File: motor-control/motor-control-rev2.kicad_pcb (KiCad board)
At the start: 2 copper layers, 122.3 x 65.9 mm, 80 parts, among them P1 CONN_02X12, P2 to_motor_phase_1, P3 to_motor_phase_2, P4 to_motor_phase_3, P5 CONN_01X01, P6 CONN_01X01, P7 CONN_01X04, Q1 csd19505kcs, Q10 csd19505kcs, Q11 csd19505kcs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

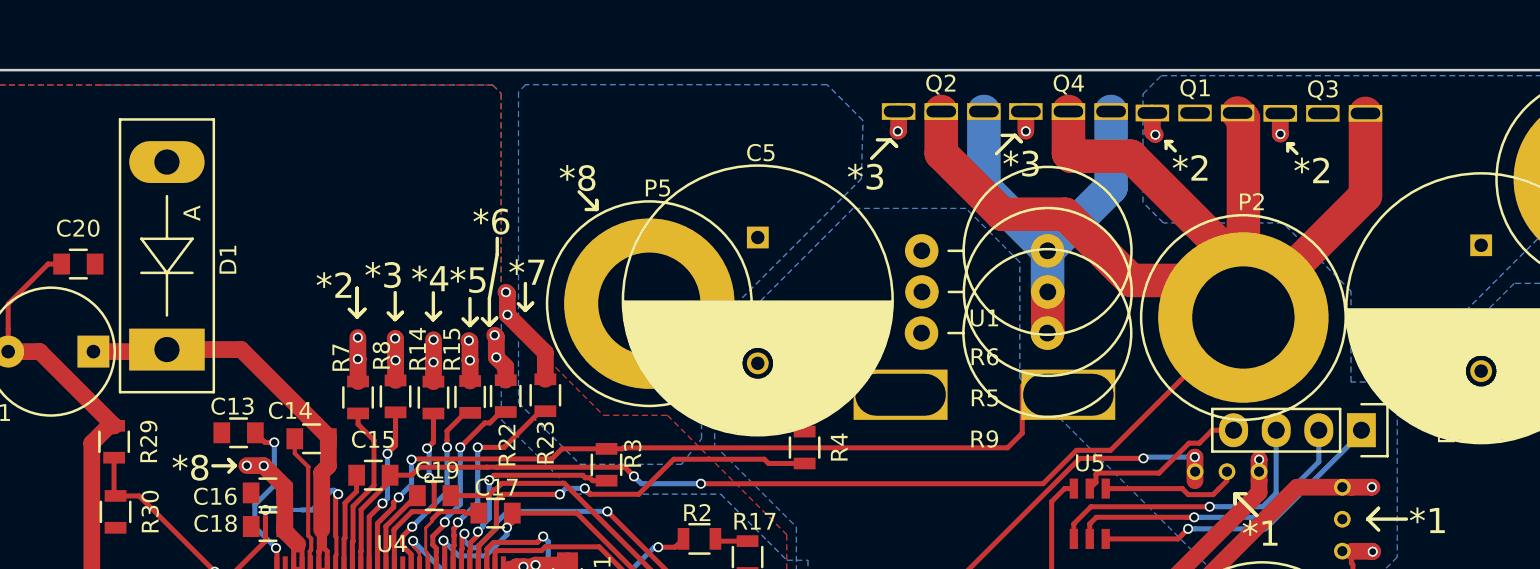
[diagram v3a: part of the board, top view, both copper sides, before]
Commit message: Started Spacing the fets
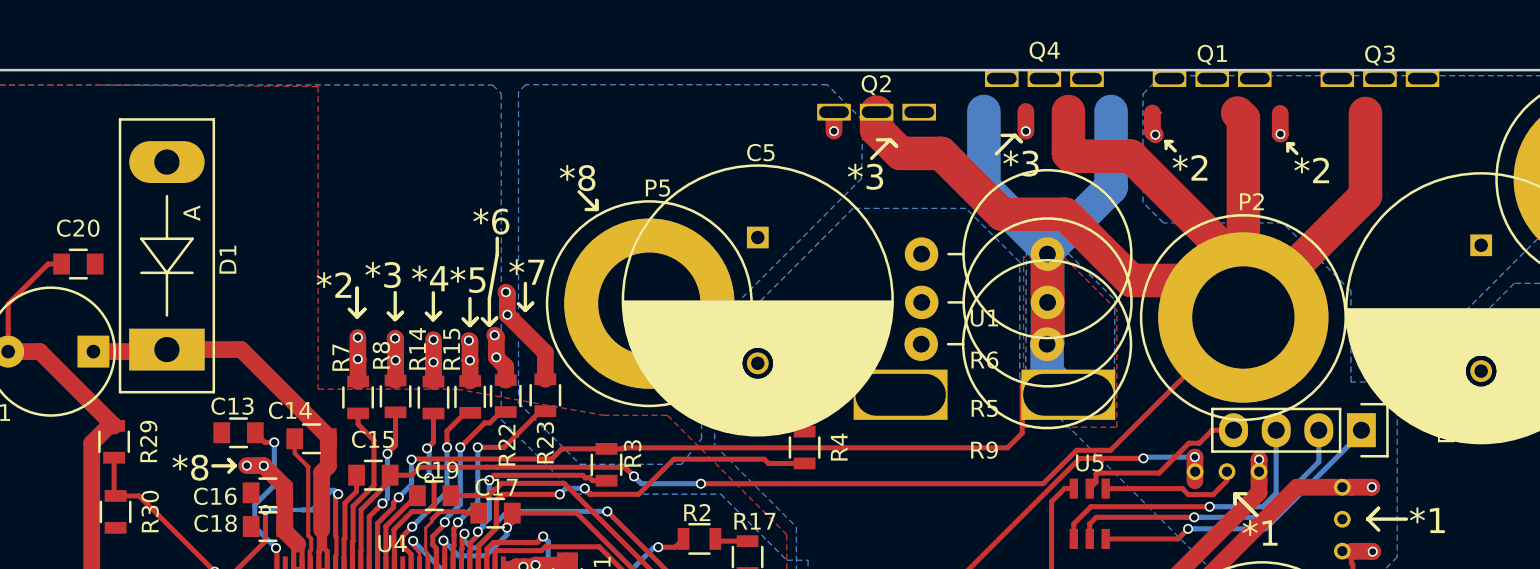
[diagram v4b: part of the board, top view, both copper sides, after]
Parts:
- moved Q3 3.98 mm to (175.0, 55.0)
- moved Q2 3.85 mm to (145.0, 57.0)
- moved Q4 2.43 mm to (155.0, 55.0)
- moved Q1 2.29 mm to (165.0, 55.0)
- moved R9 0.66 mm to (151.4, 70.8)
- moved R5 0.62 mm to (151.4, 68.3)
- moved R6 0.20 mm to (151.4, 65.5)
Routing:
- net /Gate-Driver/SL_A: track 71.9 -> 80.9 mm
- net /Gate-Driver/SH_A: track 132.8 -> 135.8 mm
- net Net-(Q1-Pad1): track 5.73 -> 7.76 mm
- net Net-(Q2-Pad1): track 4.90 -> 6.33 mm
- added copper zone on B.Cu, net /Gate-Driver/SL_A
- added copper zone on F.Cu, net /Gate-Driver/SL_A
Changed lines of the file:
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@@
   (general
     (links 228)
-    (no_connects 33)
+    (no_connects 29)
     (area 90.293999 54.419999 212.745001 120.483001)
     (thickness 1.6)
     (drawings 147)
-    (tracks 1260)
+    (tracks 1271)
     (zones 0)
     (modules 80)
@@
   )
   (setup
-    (last_trace_width 0.3)
+    (last_trace_width 2)
     (user_trace_width 0.18)
     (user_trace_width 0.3)
@@
   )
   (module p16261:csd19505kcs (layer F.Cu)
-    (at 163.9782 57.0477)
+    (at 165 55)
     (fp_text reference Q1 (at 0.0296 -1.4598) (layer F.SilkS)
       (effects (font (size 1 1) (thickness 0.15)))
@@
   )
   (module p16261:csd19505kcs (layer F.Cu)
-    (at 148.8525 56.9588)
+    (at 145 57)
     (fp_text reference Q2 (at 0.0042 -1.6503) (layer F.SilkS)
       (effects (font (size 1 1) (thickness 0.15)))
@@
   )
   (module p16261:csd19505kcs (layer F.Cu)
-    (at 171.5982 57.0731)
+    (at 175 55)
     (fp_text reference Q3 (at 0.0169 -1.4217) (layer F.SilkS)
       (effects (font (size 1 1) (thickness 0.15)))
@@
   )
   (module p16261:csd19505kcs (layer F.Cu)
-    (at 156.4344 56.9588)
+    (at 155 55)
     (fp_text reference Q4 (at 0.0169 -1.6503) (layer F.SilkS)
       (effects (font (size 1 1) (thickness 0.15)))
@@
   )
   (module Resistors_ThroughHole:Resistor_Vertical_RM7.5mm (layer F.Cu)
-    (at 151.45346 67.7157 180)
+    (at 151.44096 68.34 180)
     (descr "Resistor, Vertical, RM 7.5mm,")
     (tags "Resistor, Vertical, RM 7.5mm,")
@@
   )
   (module Resistors_ThroughHole:Resistor_Vertical_RM7.5mm (layer F.Cu)
-    (at 151.44076 65.2646 180)
+    (at 151.43096 65.46 180)
     (descr "Resistor, Vertical, RM 7.5mm,")
     (tags "Resistor, Vertical, RM 7.5mm,")
@@
   )
   (module Resistors_ThroughHole:Resistor_Vertical_RM7.5mm (layer F.Cu)
-    (at 151.42806 70.1668 180)
+    (at 151.41096 70.83 180)
     (descr "Resistor, Vertical, RM 7.5mm,")
     (tags "Resistor, Vertical, RM 7.5mm,")
@@
   (segment (start 113.257119 84.248481) (end 113.2557 84.2499) (width 0.3) (layer F.Cu) (net 13))
   (segment (start 113.315311 82.379827) (end 113.257119 82.438019) (width 0.3) (layer F.Cu) (net 13))
+  (segment (start 148.8525 59.4588) (end 146.424478 59.4588) (width 2) (layer F.Cu) (net 14))
+  (segment (start 146.424478 59.4588) (end 145 58.034322) (width 2) (layer F.Cu) (net 14))
+  (segment (start 145 58.034322) (end 145 57) (width 2) (layer F.Cu) (net 14))
   (segment (start 161.781101 74.319699) (end 166.8611 69.2397) (width 0.3) (layer F.Cu) (net 14))
   (segment (start 156.914971 77.154389) (end 158.946411 77.154389) (width 0.3) (layer F.Cu) (net 14))
@@
   (segment (start 166.8611 69.2397) (end 166.8611 66.3314) (width 2) (layer F.Cu) (net 14))
   (segment (start 152.478809 63.085109) (end 148.8525 59.4588) (width 2) (layer F.Cu) (net 14))
-  (segment (start 148.8525 59.4588) (end 148.8525 56.9588) (width 2) (layer F.Cu) (net 14))
   (segment (start 166.8611 69.2397) (end 166.8611 57.3906) (width 2) (layer F.Cu) (net 14))
   (segment (start 166.8611 57.3906) (end 166.5182 57.0477) (width 2) (layer F.Cu) (net 14))
@@
   (segment (start 121.7557 103.468162) (end 121.7557 96.219717) (width 0.3) (layer F.Cu) (net 42))
   (segment (start 122.034388 95.941029) (end 122.034387 94.93857) (width 0.3) (layer F.Cu) (net 42))
-  (segment (start 114.0799 71.7162) (end 114.0799 70.4335) (width 1) (layer F.Cu) (net 43))
-  (via (at 114.0799 70.4335) (size 0.6) (drill 0.4) (layers F.Cu B.Cu) (net 43))
-  (segment (start 114.0926 73.0547) (end 114.0926 71.7289) (width 1) (layer F.Cu) (net 43))
-  (segment (start 114.0926 71.7289) (end 114.0799 71.7162) (width 1) (layer F.Cu) (net 43))
   (via (at 114.0799 71.7162) (size 0.6) (drill 0.4) (layers F.Cu B.Cu) (net 43))
+  (segment (start 114.0926 71.7289) (end 114.0799 71.7162) (width 1) (layer F.Cu) (net 43))
+  (segment (start 114.0926 73.0547) (end 114.0926 71.7289) (width 1) (layer F.Cu) (net 43))
+  (via (at 114.0799 70.4335) (size 0.6) (drill 0.4) (layers F.Cu B.Cu) (net 43))
+  (segment (start 114.0799 71.7162) (end 114.0799 70.4335) (width 1) (layer F.Cu) (net 43))
+  (segment (start 169.0709 58.305) (end 169.0709 57.556078) (width 0.3) (layer F.Cu) (net 43))
+  (segment (start 169.0709 57.556078) (end 168.72 57.205178) (width 0.3) (layer F.Cu) (net 43))
+  (segment (start 161.616 58.3431) (end 161.616 57.556078) (width 0.3) (layer F.Cu) (net 43))
   (segment (start 161.4382 57.0477) (end 161.4382 58.1653) (width 1) (layer F.Cu) (net 43))
   (segment (start 161.4382 58.1653) (end 161.616 58.3431) (width 1) (layer F.Cu) (net 43))
@@
   (via (at 169.0709 58.305) (size 0.6) (drill 0.4) (layers F.Cu B.Cu) (net 43))
   (segment (start 161.9382 57.0477) (end 161.4382 57.0477) (width 0.18) (layer F.Cu) (net 43))
+  (segment (start 155.16 70.83) (end 155.16 72.5752) (width 2) (layer B.Cu) (net 44))
+  (segment (start 155.16 72.5752) (end 156.4285 73.8437) (width 2) (layer B.Cu) (net 44))
+  (segment (start 155.19 68.34) (end 155.19 70.8) (width 2) (layer B.Cu) (net 44))
+  (segment (start 155.19 70.8) (end 155.16 70.83) (width 2) (layer B.Cu) (net 44))
+  (segment (start 155.18 65.46) (end 155.18 68.33) (width 2) (layer F.Cu) (net 44))
+  (segment (start 155.18 68.33) (end 155.19 68.34) (width 2) (layer F.Cu) (net 44))
   (segment (start 115.2557 83.1749) (end 115.2557 84.2499) (width 0.3) (layer F.Cu) (net 44))
   (segment (start 116.5183 79.9585) (end 116.218301 80.258499) (width 0.3) (layer F.Cu) (net 44))
@@
   (segment (start 155.1898 65.2646) (end 158.9744 61.48) (width 2) (layer B.Cu) (net 44))
   (segment (start 158.9744 61.48) (end 158.9744 56.9588) (width 2) (layer B.Cu) (net 44))
-  (segment (start 116.3278 71.7924) (end 116.3278 70.5097) (width 1) (layer F.Cu) (net 45))
-  (segment (start 116.3278 70.5097) (end 116.3024 70.4843) (width 1) (layer F.Cu) (net 45))
-  (via (at 116.3024 70.4843) (size 0.6) (drill 0.4) (layers F.Cu B.Cu) (net 45))
-  (segment (start 116.3278 72.9912) (end 116.3278 71.7924) (width 1) (layer F.Cu) (net 45))
+  (via (at 142.46 58.1303) (size 0.6) (drill 0.4) (layers F.Cu B.Cu) (net 45))
+  (segment (start 142.46 57) (end 142.46 58.1303) (width 1) (layer F.Cu) (net 45))
   (via (at 116.3278 71.7924) (size 0.6) (drill 0.4) (layers F.Cu B.Cu) (net 45))
-  (segment (start 146.3125 56.9588) (end 146.3125 58.0891) (width 1) (layer F.Cu) (net 45))
-  (segment (start 146.3125 58.0891) (end 146.2617 58.1399) (width 1) (layer F.Cu) (net 45))
-  (via (at 146.2617 58.1399) (size 0.6) (drill 0.4) (layers F.Cu B.Cu) (net 45))
+  (segment (start 116.3278 72.9912) (end 116.3278 71.7924) (width 1) (layer F.Cu) (net 45))
+  (via (at 116.3024 70.4843) (size 0.6) (drill 0.4) (layers F.Cu B.Cu) (net 45))
+  (segment (start 116.3278 70.5097) (end 116.3024 70.4843) (width 1) (layer F.Cu) (net 45))
+  (segment (start 116.3278 71.7924) (end 116.3278 70.5097) (width 1) (layer F.Cu) (net 45))
+  (segment (start 153.8944 58.1399) (end 153.8944 56.6344) (width 0.3) (layer F.Cu) (net 45))
   (segment (start 153.8944 56.9588) (end 153.8944 58.1399) (width 1) (layer F.Cu) (net 45))
   (via (at 153.8944 58.1399) (size 0.6) (drill 0.4) (layers F.Cu B.Cu) (net 45))
@@
     (polygon
       (pts
-        (xy 162.71328 66.00882) (xy 160.60508 66.00882) (xy 156.66046 62.0642) (xy 152.90888 62.0642) (xy 149.8939 59.04922)
-        (xy 149.8939 57.56586) (xy 147.8365 57.56586) (xy 147.8365 59.89758) (xy 152.04528 64.10636) (xy 155.7994 64.10636)
+        (xy 162.71328 66.00882) (xy 160.60508 66.00882) (xy 156.66046 62.0642) (xy 152.90888 62.0642) (xy 149.9 59.1)
+        (xy 149.2 58.4) (xy 146.8 58.4) (xy 146.1 57.7) (xy 146.1 57.5) (xy 144 57.5)
+        (xy 144 58.5) (xy 146 60.5) (xy 148.5 60.5) (xy 152.04528 64.10636) (xy 155.7994 64.10636)
         (xy 159.75418 68.06114) (xy 162.08082 68.06114) (xy 162.9241 67.21786) (xy 162.9241 66.21964)
       )
@@
     (polygon
       (pts
-        (xy 98.751 55.384) (xy 122.119 55.384) (xy 122.627 55.892) (xy 122.627 68.973) (xy 128.723 75.069)
+        (xy 98.751 55.384) (xy 111.70928 55.47) (xy 111.71 73.51) (xy 120 73.51) (xy 128.723 75.069)
         (xy 132.533 75.069) (xy 139.645 82.181) (xy 139.645 85.864) (xy 129.993 95.516) (xy 129.993 103.771)
         (xy 131.136 104.914) (xy 131.136 105.422) (xy 130.882 105.676) (xy 123.008 105.676) (xy 122.5 106.184)
@@
       )
     )
+  )
+  (zone (net 44) (net_name /Gate-Driver/SL_A) (layer B.Cu) (hatch edge 0.508)
+    (connect_pads yes (clearance 0.508))
+    (min_thickness 0.254)
+    (fill yes (arc_segments 16) (thermal_gap 0.508) (thermal_bridge_width 0.508))
+    (polygon
+      (pts
+        (xy 159.2 68.19) (xy 159.17 73.04) (xy 153.89 73.04) (xy 153.92 65.43) (xy 156.44 65.43)
+        (xy 159.2 68.19)
+      )
+    )
+  )
+  (zone (net 0) (net_name "") (layer B.Mask) (hatch edge 0.508)
+    (connect_pads yes (clearance 0.508))
+    (min_thickness 0.254)
+    (fill yes (arc_segments 16) (thermal_gap 0.508) (thermal_bridge_width 0.508))
+    (polygon
+      (pts
+        (xy 154 65.62) (xy 154 72.48) (xy 159.05 72.48) (xy 159.05 68.19) (xy 156.48 65.62)
+      )
+    )
+  )
+  (zone (net 44) (net_name /Gate-Driver/SL_A) (layer F.Cu) (hatch edge 0.508)
+    (connect_pads yes (clearance 0.508))
+    (min_thickness 0.254)
+    (fill yes (arc_segments 16) (thermal_gap 0.508) (thermal_bridge_width 0.508))
+    (polygon
+      (pts
+        (xy 153.76 65.61) (xy 153.76 75.35) (xy 153.76 75.78) (xy 159.32 75.78) (xy 159.32 68.8)
+        (xy 156.16 65.64) (xy 153.76 65.64)
+      )
+    )

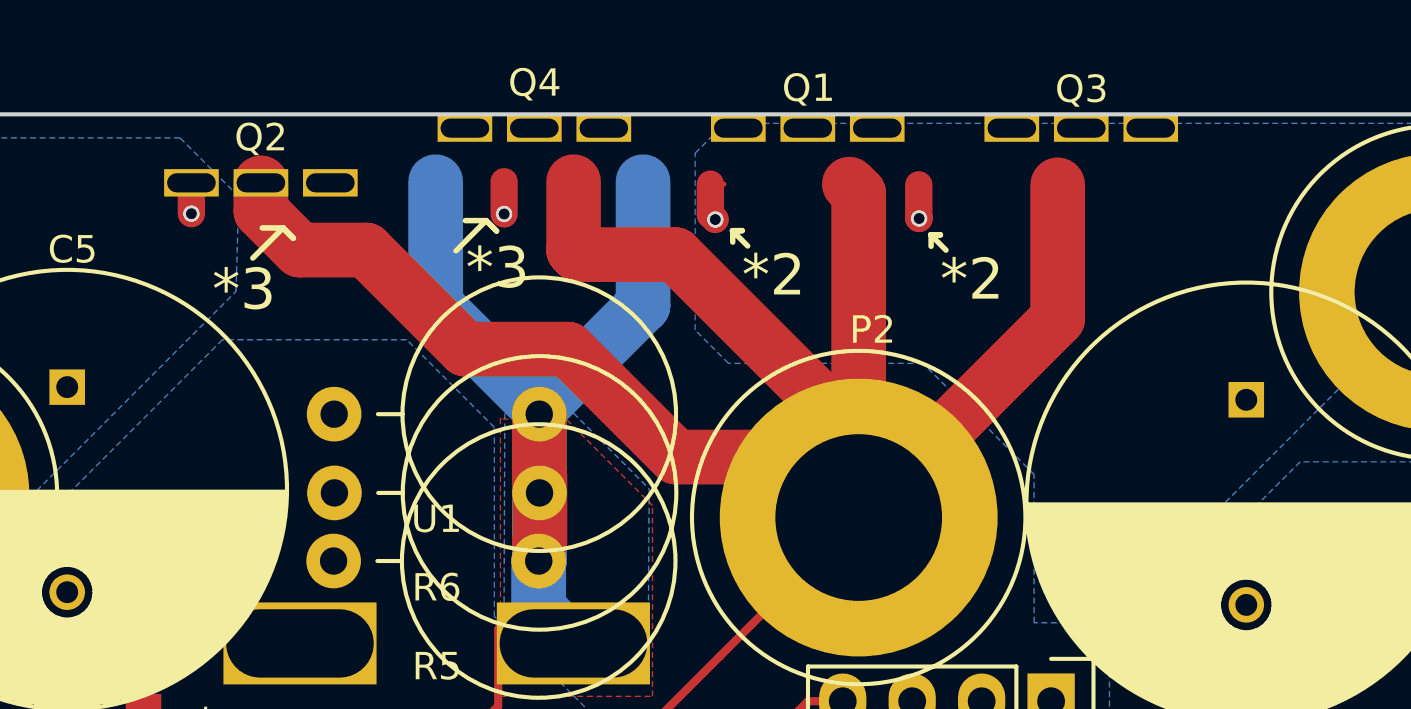
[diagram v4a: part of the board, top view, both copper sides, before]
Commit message: Continued FET movement and spacing 1st reg good
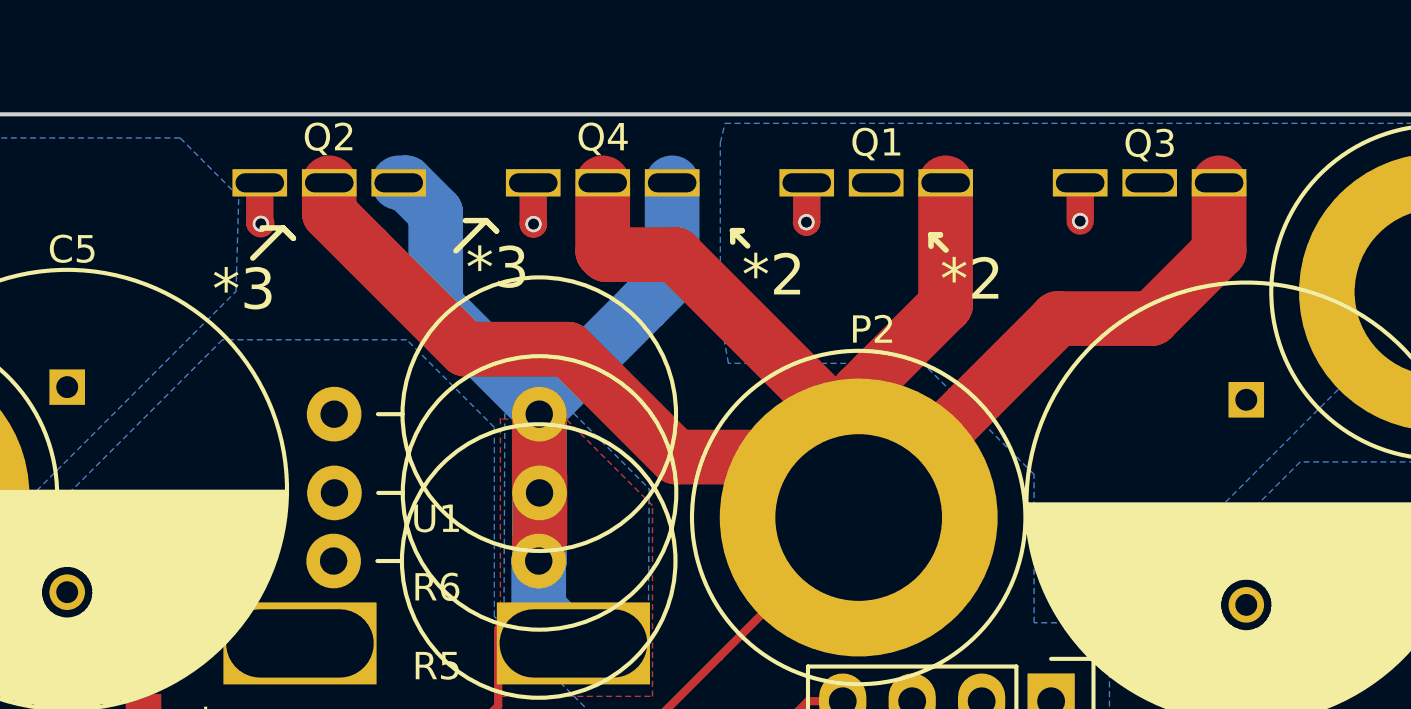
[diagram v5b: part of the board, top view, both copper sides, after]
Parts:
- moved Q1 3.20 mm to (167.5, 57.0)
- moved Q3 3.20 mm to (177.5, 57.0)
- moved Q4 3.20 mm to (157.5, 57.0)
- moved Q2 2.50 mm to (147.5, 57.0)
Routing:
- net Net-(Q1-Pad1): track 7.76 -> 5.47 mm
- net /Gate-Driver/SH_A: track 135.8 -> 138.0 mm
- net /Gate-Driver/SL_A: track 80.9 -> 81.9 mm
- net Net-(Q2-Pad1): track 6.33 -> 5.55 mm
